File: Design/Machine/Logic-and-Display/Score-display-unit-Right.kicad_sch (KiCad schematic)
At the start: 5 parts, among them M5 Red, M6 Red, M7 Red, M8 Red

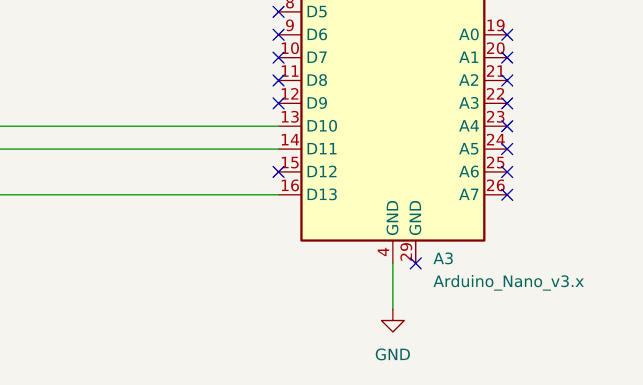
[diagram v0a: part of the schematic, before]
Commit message: fix: scores MCU GNDs
connect all Nano's GNDs to GND on right and left score schematics
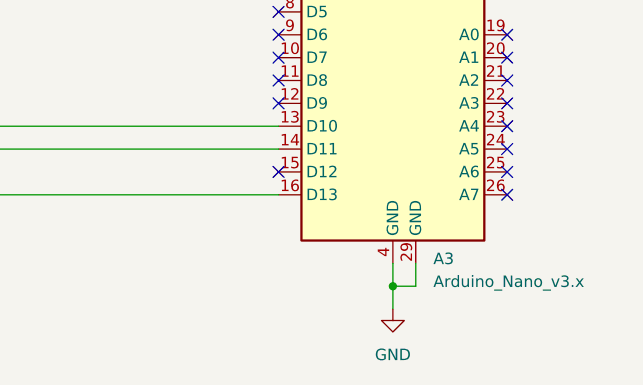
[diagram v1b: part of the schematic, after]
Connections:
- net GND: now also A3.29 (GND)
- no-connect marks 29 -> 28
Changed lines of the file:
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@@
 (kicad_sch (version 20230121) (generator eeschema)
   (paper "A4")
+  (junction (at 205.74 127) (diameter 0) (color 0 0 0 0)
+  )
   (no_connect (at 218.44 99.06))
   (no_connect (at 193.04 114.3))
@@
   (no_connect (at 210.82 73.66))
   (no_connect (at 193.04 101.6))
-  (no_connect (at 208.28 124.46))
   (wire (pts (xy 132.08 88.9) (xy 137.16 88.9))
     (stroke (width 0) (type default))
@@
     (stroke (width 0) (type default))
   )
+  (wire (pts (xy 205.74 127) (xy 205.74 129.54))
+    (stroke (width 0) (type default))
+  )
   (wire (pts (xy 106.68 91.44) (xy 111.76 91.44))
     (stroke (width 0) (type default))
@@
     (stroke (width 0) (type default))
   )
-  (wire (pts (xy 205.74 124.46) (xy 205.74 129.54))
+  (wire (pts (xy 205.74 124.46) (xy 205.74 127))
     (stroke (width 0) (type default))
   )
@@
   )
   (wire (pts (xy 53.34 91.44) (xy 60.96 91.44))
+    (stroke (width 0) (type default))
+  )
+  (wire (pts (xy 208.28 124.46) (xy 208.28 127))
     (stroke (width 0) (type default))
   )
@@
     (stroke (width 0) (type default))
   )
+  (wire (pts (xy 208.28 127) (xy 205.74 127))
+    (stroke (width 0) (type default))
+  )
   (wire (pts (xy 193.04 111.76) (xy 53.34 111.76))
     (stroke (width 0) (type default))
@@
     (effects (font (size 1.27 1.27)) (justify right))
   )
-  (symbol (lib_id "Arduino modules:8x8_LED_Matrix_MAX7219") (at 121.92 81.28 0) (unit 1)
+  (symbol (lib_name "8x8_LED_Matrix_MAX7219_3") (lib_id "Arduino modules:8x8_LED_Matrix_MAX7219") (at 121.92 81.28 0) (unit 1)
     (in_bom yes) (on_board yes) (dnp no)
     (property "Reference" "M7" (at 121.92 81.026 0)

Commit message: feat: display units schematics
complete all display units schematics, this is left and right scores units; and LEDs, timer, and period display unit
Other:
- title: (none) -> Right score display unit schematic
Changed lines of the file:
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@@
 (kicad_sch (version 20230121) (generator eeschema)
   (paper "A4")
+  (title_block
+    (title "Right score display unit schematic")
+    (date "2023-05-19")
+    (rev "1.0.0")
+    (comment 1 "Connection to logic unit pending")
+  )
   (junction (at 205.74 127) (diameter 0) (color 0 0 0 0)
   )

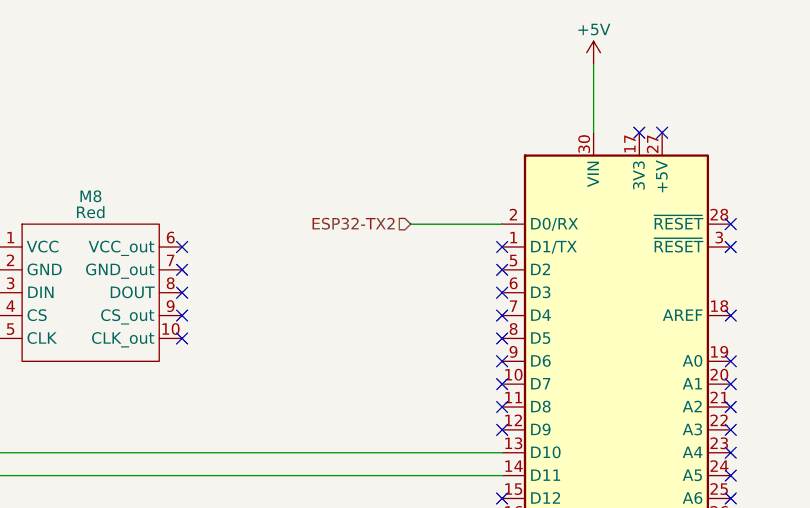
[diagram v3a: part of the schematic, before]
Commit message: feat: logic unit schematics
make schematics for logic unit, power redundancy unit still missing
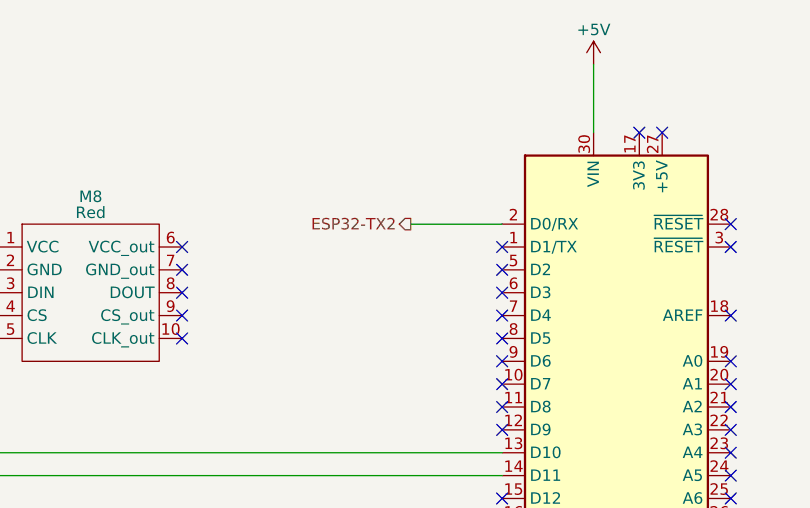
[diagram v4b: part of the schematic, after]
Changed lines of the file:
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@@
     (stroke (width 0) (type default))
   )
-  (hierarchical_label "ESP32-TX2" (shape input) (at 182.88 83.82 180) (fields_autoplaced)
+  (hierarchical_label "ESP32-TX2" (shape output) (at 182.88 83.82 180) (fields_autoplaced)
     (effects (font (size 1.27 1.27)) (justify right))
   )

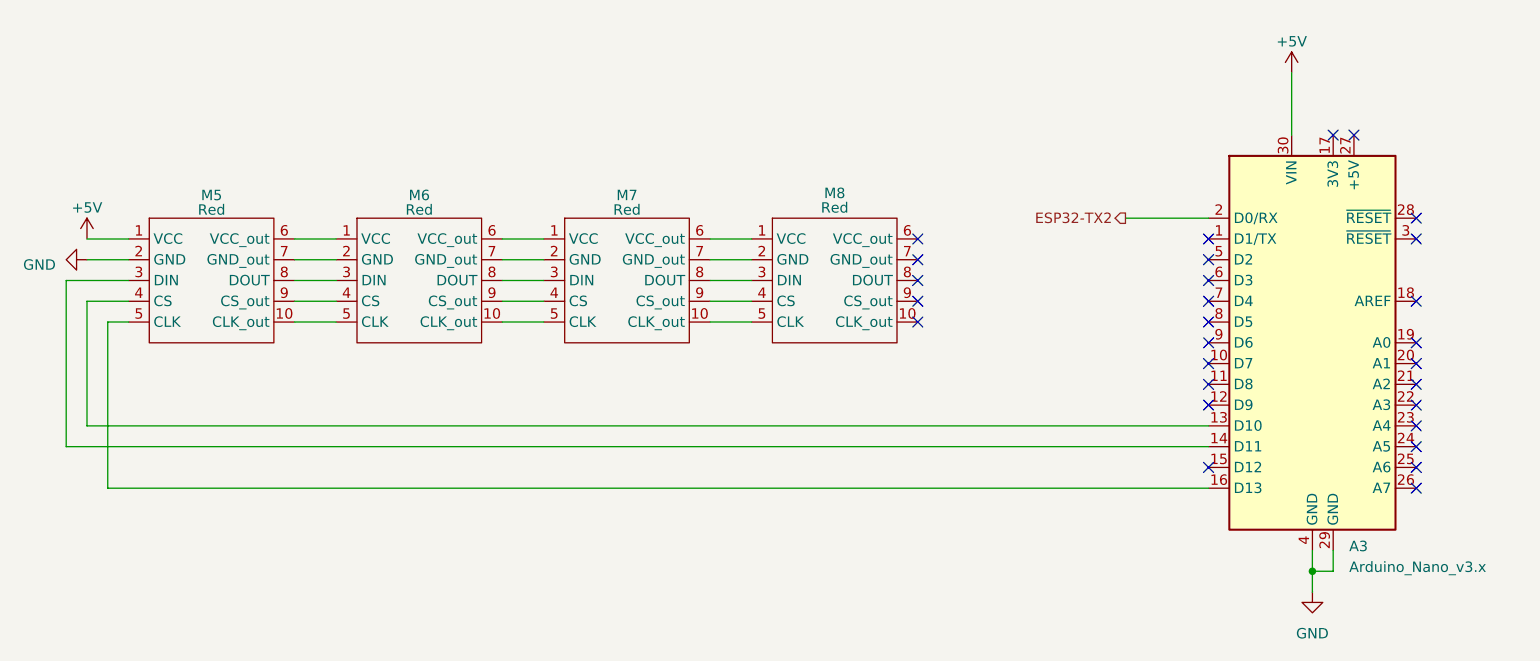
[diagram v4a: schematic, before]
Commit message: feat: logic and display units schecmatics
complete logic and display units schematics
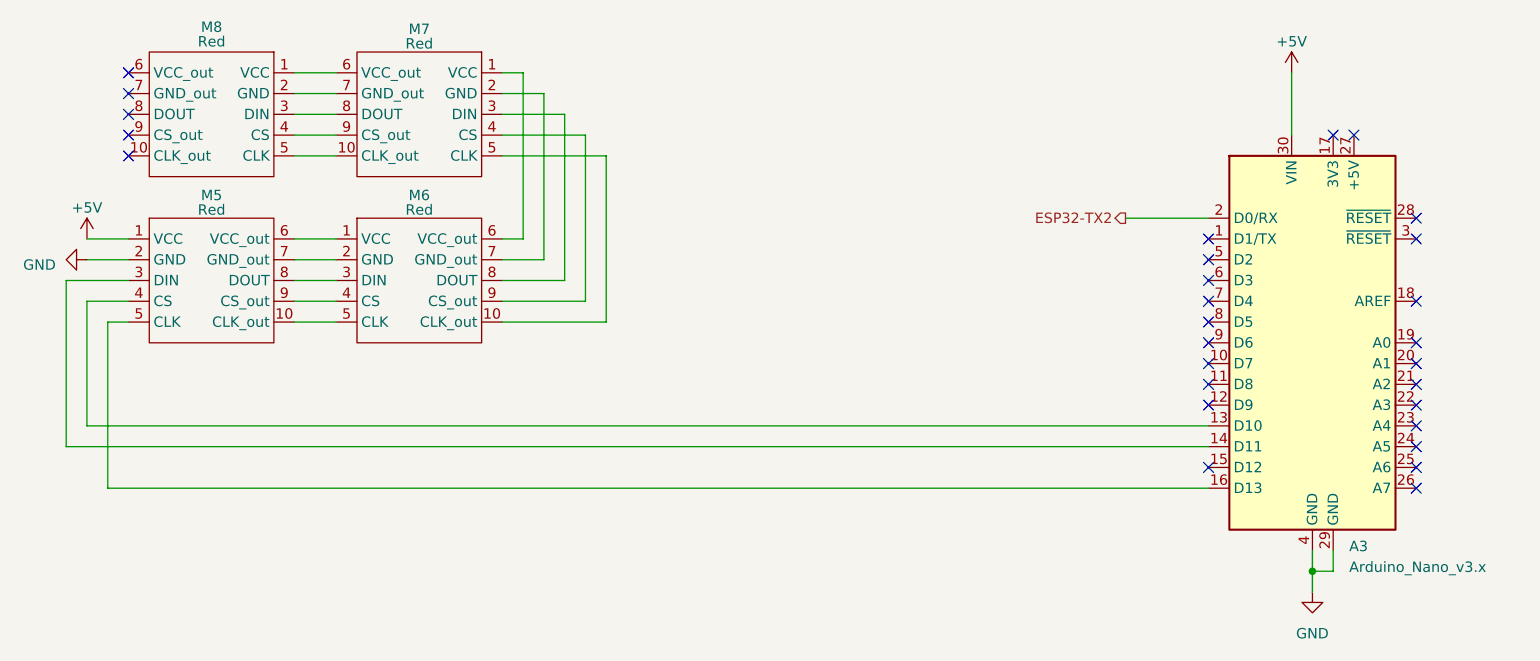
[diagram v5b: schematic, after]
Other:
- moved on the sheet: M7, M8
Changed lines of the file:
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@@
   (title_block
     (title "Right score display unit schematic")
-    (date "2023-05-19")
-    (rev "1.0.0")
+    (date "2023-06-14")
+    (rev "1.0.1")
     (comment 1 "Connection to logic unit pending")
   )
@@
   (no_connect (at 218.44 99.06))
   (no_connect (at 193.04 114.3))
+  (no_connect (at 60.96 73.66))
   (no_connect (at 218.44 111.76))
-  (no_connect (at 157.48 91.44))
-  (no_connect (at 157.48 88.9))
-  (no_connect (at 157.48 86.36))
+  (no_connect (at 60.96 66.04))
+  (no_connect (at 60.96 76.2))
   (no_connect (at 218.44 86.36))
   (no_connect (at 193.04 86.36))
@@
   (no_connect (at 218.44 104.14))
   (no_connect (at 218.44 101.6))
-  (no_connect (at 157.48 96.52))
   (no_connect (at 193.04 93.98))
+  (no_connect (at 60.96 71.12))
   (no_connect (at 193.04 91.44))
   (no_connect (at 218.44 109.22))
@@
   (no_connect (at 193.04 104.14))
   (no_connect (at 193.04 99.06))
+  (no_connect (at 60.96 68.58))
   (no_connect (at 218.44 116.84))
-  (no_connect (at 157.48 93.98))
   (no_connect (at 193.04 96.52))
   (no_connect (at 218.44 114.3))
   (no_connect (at 210.82 73.66))
   (no_connect (at 193.04 101.6))
-  (wire (pts (xy 132.08 88.9) (xy 137.16 88.9))
+  (wire (pts (xy 116.84 93.98) (xy 116.84 73.66))
+    (stroke (width 0) (type default))
+  )
+  (wire (pts (xy 109.22 66.04) (xy 106.68 66.04))
     (stroke (width 0) (type default))
   )
@@
     (stroke (width 0) (type default))
   )
-  (wire (pts (xy 106.68 96.52) (xy 111.76 96.52))
+  (wire (pts (xy 106.68 93.98) (xy 116.84 93.98))
     (stroke (width 0) (type default))
   )
@@
     (stroke (width 0) (type default))
   )
+  (wire (pts (xy 106.68 86.36) (xy 109.22 86.36))
+    (stroke (width 0) (type default))
+  )
   (wire (pts (xy 55.88 88.9) (xy 60.96 88.9))
     (stroke (width 0) (type default))
@@
     (stroke (width 0) (type default))
   )
-  (wire (pts (xy 106.68 86.36) (xy 111.76 86.36))
-    (stroke (width 0) (type default))
-  )
-  (wire (pts (xy 132.08 96.52) (xy 137.16 96.52))
+  (wire (pts (xy 81.28 76.2) (xy 86.36 76.2))
+    (stroke (width 0) (type default))
+  )
+  (wire (pts (xy 106.68 88.9) (xy 111.76 88.9))
     (stroke (width 0) (type default))
   )
@@
     (stroke (width 0) (type default))
   )
-  (wire (pts (xy 106.68 91.44) (xy 111.76 91.44))
-    (stroke (width 0) (type default))
-  )
-  (wire (pts (xy 132.08 86.36) (xy 137.16 86.36))
+  (wire (pts (xy 81.28 71.12) (xy 86.36 71.12))
     (stroke (width 0) (type default))
   )
@@
     (stroke (width 0) (type default))
   )
+  (wire (pts (xy 109.22 86.36) (xy 109.22 66.04))
+    (stroke (width 0) (type default))
+  )
   (wire (pts (xy 193.04 116.84) (xy 58.42 116.84))
     (stroke (width 0) (type default))
   )
+  (wire (pts (xy 114.3 71.12) (xy 106.68 71.12))
+    (stroke (width 0) (type default))
+  )
   (wire (pts (xy 55.88 93.98) (xy 60.96 93.98))
     (stroke (width 0) (type default))
@@
     (stroke (width 0) (type default))
   )
+  (wire (pts (xy 111.76 88.9) (xy 111.76 68.58))
+    (stroke (width 0) (type default))
+  )
   (wire (pts (xy 81.28 91.44) (xy 86.36 91.44))
     (stroke (width 0) (type default))
   )
+  (wire (pts (xy 114.3 91.44) (xy 114.3 71.12))
+    (stroke (width 0) (type default))
+  )
   (wire (pts (xy 58.42 96.52) (xy 60.96 96.52))
     (stroke (width 0) (type default))
@@
     (stroke (width 0) (type default))
   )
+  (wire (pts (xy 119.38 96.52) (xy 119.38 76.2))
+    (stroke (width 0) (type default))
+  )
   (wire (pts (xy 53.34 91.44) (xy 60.96 91.44))
     (stroke (width 0) (type default))
@@
     (stroke (width 0) (type default))
   )
+  (wire (pts (xy 111.76 68.58) (xy 106.68 68.58))
+    (stroke (width 0) (type default))
+  )
+  (wire (pts (xy 106.68 91.44) (xy 114.3 91.44))
+    (stroke (width 0) (type default))
+  )
   (wire (pts (xy 203.2 66.04) (xy 203.2 73.66))
     (stroke (width 0) (type default))
@@
     (stroke (width 0) (type default))
   )
-  (wire (pts (xy 106.68 93.98) (xy 111.76 93.98))
-    (stroke (width 0) (type default))
-  )
-  (wire (pts (xy 132.08 93.98) (xy 137.16 93.98))
-    (stroke (width 0) (type default))
-  )
   (wire (pts (xy 55.88 109.22) (xy 55.88 93.98))
     (stroke (width 0) (type default))
@@
     (stroke (width 0) (type default))
   )
-  (wire (pts (xy 132.08 91.44) (xy 137.16 91.44))
+  (wire (pts (xy 116.84 73.66) (xy 106.68 73.66))
     (stroke (width 0) (type default))
   )
@@
     (stroke (width 0) (type default))
   )
+  (wire (pts (xy 81.28 73.66) (xy 86.36 73.66))
+    (stroke (width 0) (type default))
+  )
   (wire (pts (xy 208.28 127) (xy 205.74 127))
     (stroke (width 0) (type default))
@@
     (stroke (width 0) (type default))
   )
-  (wire (pts (xy 106.68 88.9) (xy 111.76 88.9))
+  (wire (pts (xy 81.28 68.58) (xy 86.36 68.58))
+    (stroke (width 0) (type default))
+  )
+  (wire (pts (xy 106.68 96.52) (xy 119.38 96.52))
+    (stroke (width 0) (type default))
+  )
+  (wire (pts (xy 81.28 66.04) (xy 86.36 66.04))
+    (stroke (width 0) (type default))
+  )
+  (wire (pts (xy 119.38 76.2) (xy 106.68 76.2))
     (stroke (width 0) (type default))
   )
@@
     (effects (font (size 1.27 1.27)) (justify right))
   )
-  (symbol (lib_name "8x8_LED_Matrix_MAX7219_3") (lib_id "Arduino modules:8x8_LED_Matrix_MAX7219") (at 121.92 81.28 0) (unit 1)
+  (symbol (lib_name "8x8_LED_Matrix_MAX7219_3") (lib_id "Arduino modules:8x8_LED_Matrix_MAX7219") (at 96.52 60.96 0) (mirror y) (unit 1)
     (in_bom yes) (on_board yes) (dnp no)
-    (property "Reference" "M7" (at 121.92 81.026 0)
-      (effects (font (size 1.27 1.27)))
-    )
-    (property "Value" "Red" (at 121.92 82.804 0)
-      (effects (font (size 1.27 1.27)))
-    )
-    (property "Footprint" "" (at 121.92 81.28 0)
-      (effects (font (size 1.27 1.27)) hide)
-    )
-    (property "Datasheet" "" (at 121.92 81.28 0)
+    (property "Reference" "M7" (at 96.52 60.706 0)
+      (effects (font (size 1.27 1.27)))
+    )
+    (property "Value" "Red" (at 96.52 62.484 0)
+      (effects (font (size 1.27 1.27)))
+    )
+    (property "Footprint" "" (at 96.52 60.96 0)
+      (effects (font (size 1.27 1.27)) hide)
+    )
+    (property "Datasheet" "" (at 96.52 60.96 0)
       (effects (font (size 1.27 1.27)) hide)
     )
@@
     )
   )
-  (symbol (lib_id "Arduino modules:8x8_LED_Matrix_MAX7219") (at 147.32 81.28 0) (unit 1)
+  (symbol (lib_id "Arduino modules:8x8_LED_Matrix_MAX7219") (at 71.12 60.96 0) (mirror y) (unit 1)
     (in_bom yes) (on_board yes) (dnp no)
-    (property "Reference" "M8" (at 147.32 80.772 0)
-      (effects (font (size 1.27 1.27)))
-    )
-    (property "Value" "Red" (at 147.32 82.55 0)
-      (effects (font (size 1.27 1.27)))
-    )
-    (property "Footprint" "" (at 147.32 81.28 0)
-      (effects (font (size 1.27 1.27)) hide)
-    )
-    (property "Datasheet" "" (at 147.32 81.28 0)
-      (effects (font (size 1.27 1.27)) hide)
-    )
+    (property "Reference" "M8" (at 71.12 60.452 0)
+      (effects (font (size 1.27 1.27)))
+    )
+    (property "Value" "Red" (at 71.12 62.23 0)
+      (effects (font (size 1.27 1.27)))
+    )
+    (property "Footprint" "" (at 71.12 60.96 0)
+      (effects (font (size 1.27 1.27)) hide)
+    )
+    (property "Datasheet" "" (at 71.12 60.96 0)
+      (effects (font (size 1.27 1.27)) hide)
+    )

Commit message: fix: set FC-16 hardware module variable
set hardware variable as FC-16, this stops flipping of the lower zone, fix wiring diagram to represent this
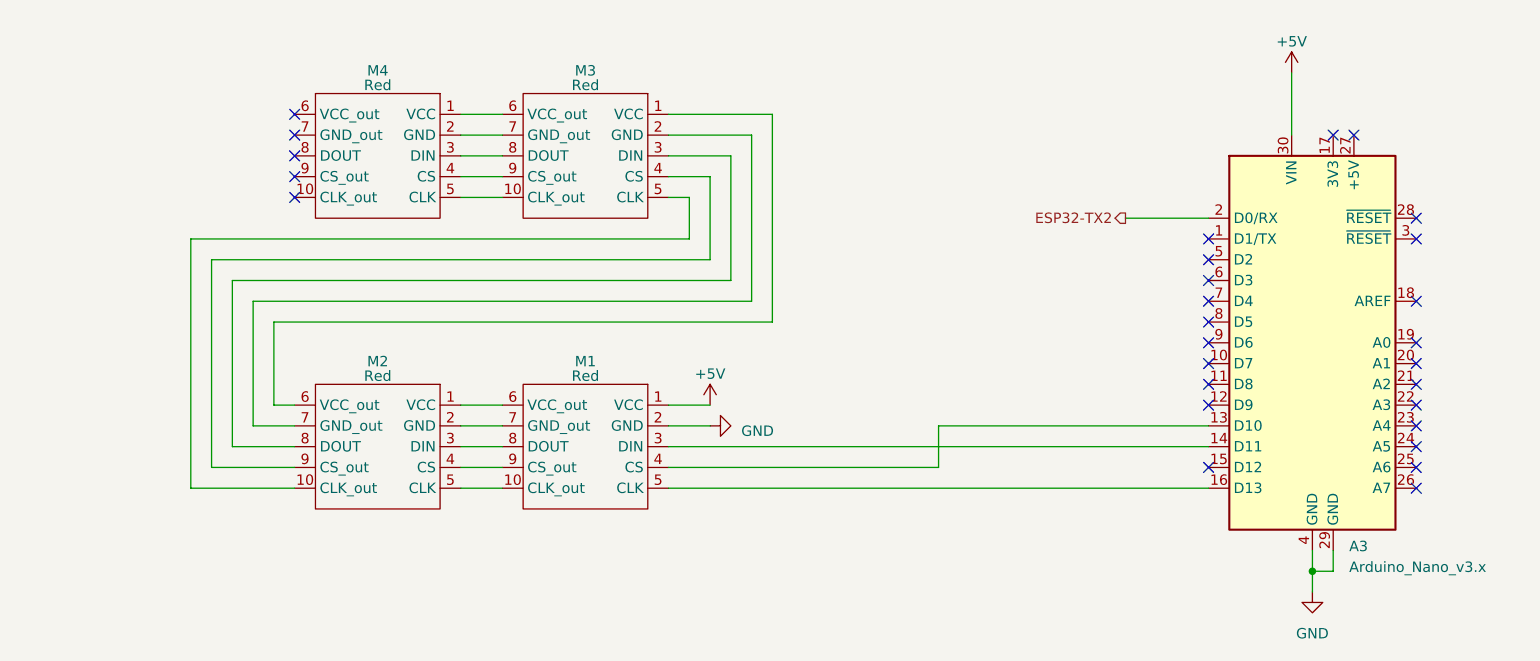
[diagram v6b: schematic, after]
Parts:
- removed M5: Red, Connector_PinSocket_2.54mm:PinSocket_1x05_P2.54mm_Vertical, symbol Arduino modules:8x8_LED_Matrix_MAX7219
- removed M6, M7, M8: Red, symbol Arduino modules:8x8_LED_Matrix_MAX7219
- added M1: Red, Connector_PinSocket_2.54mm:PinSocket_1x05_P2.54mm_Vertical, symbol Arduino modules:8x8_LED_Matrix_MAX7219
- added M2, M3, M4: Red, symbol Arduino modules:8x8_LED_Matrix_MAX7219
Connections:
- net +5V: now also M1.1 (VCC)
- net GND: now also M1.2 (GND)
- net at A3.13 (D10): now also M1.4 (CS)
- net at A3.14 (D11): now also M1.3 (DIN)
- net at A3.16 (D13): now also M1.5 (CLK)
- new net: M1.10 (CLK_out), M2.5 (CLK)
- new net: M1.6 (VCC_out), M2.1 (VCC)
- new net: M1.7 (GND_out), M2.2 (GND)
- new net: M1.8 (DOUT), M2.3 (DIN)
- new net: M1.9 (CS_out), M2.4 (CS)
- new net: M2.10 (CLK_out), M3.5 (CLK)
- new net: M2.6 (VCC_out), M3.1 (VCC)
- new net: M2.7 (GND_out), M3.2 (GND)
- new net: M2.8 (DOUT), M3.3 (DIN)
- new net: M2.9 (CS_out), M3.4 (CS)
- new net: M3.6 (VCC_out), M4.1 (VCC)
- new net: M3.7 (GND_out), M4.2 (GND)
- new net: M3.8 (DOUT), M4.3 (DIN)
- new net: M3.9 (CS_out), M4.4 (CS)
- new net: M3.10 (CLK_out), M4.5 (CLK)
